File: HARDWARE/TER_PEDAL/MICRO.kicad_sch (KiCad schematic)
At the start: 23 parts, among them J7 DEBUG, SW1 RST, U1 STM32F103C8Tx, Y1 8mHz

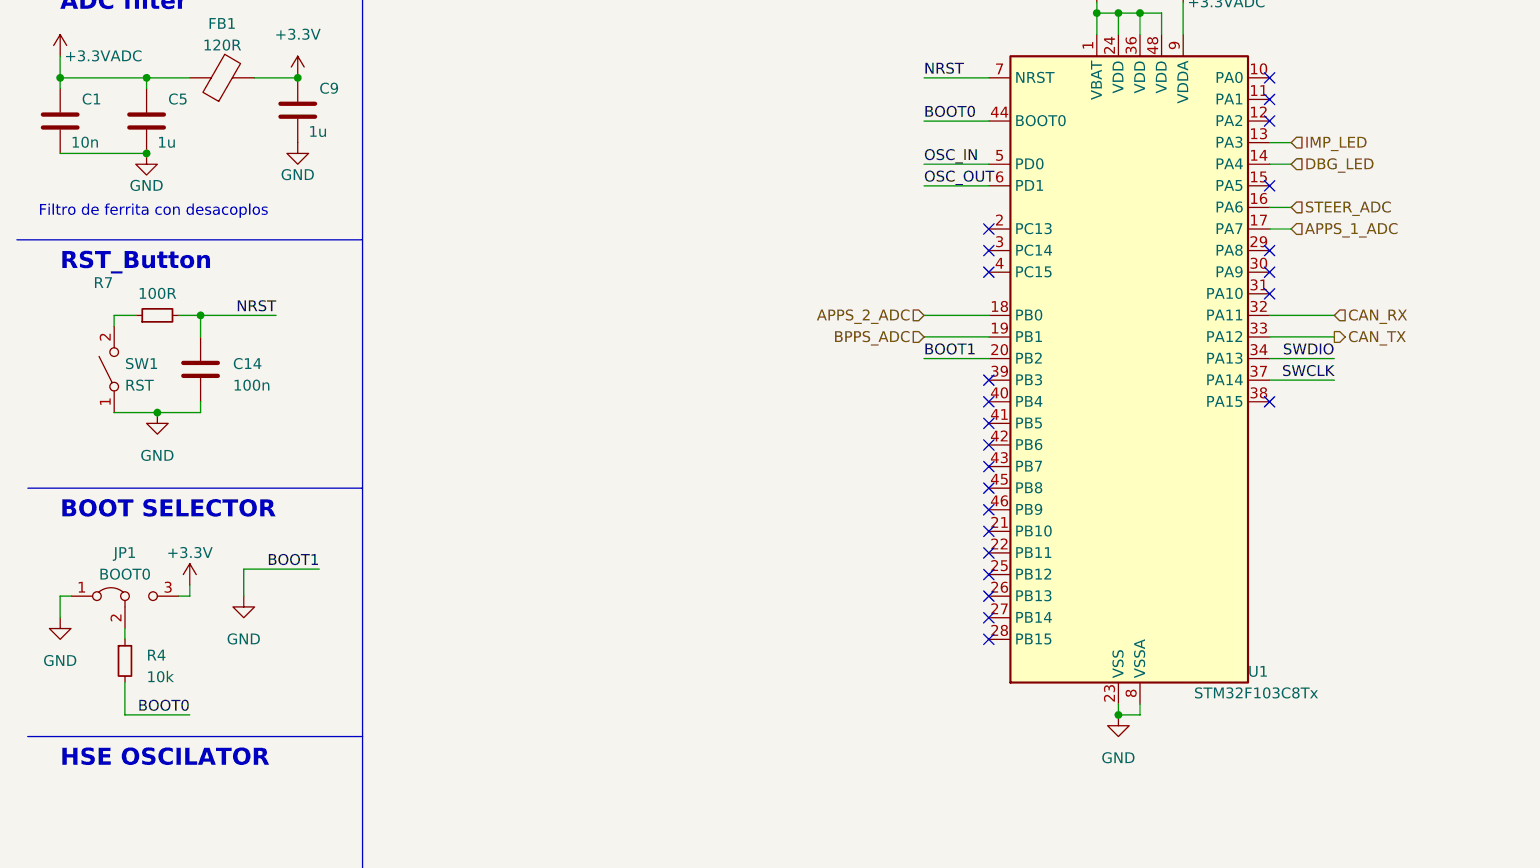
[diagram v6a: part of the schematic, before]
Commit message: Added voltage followers to sensing, improved can circuitri, improved layout, waiting for routing
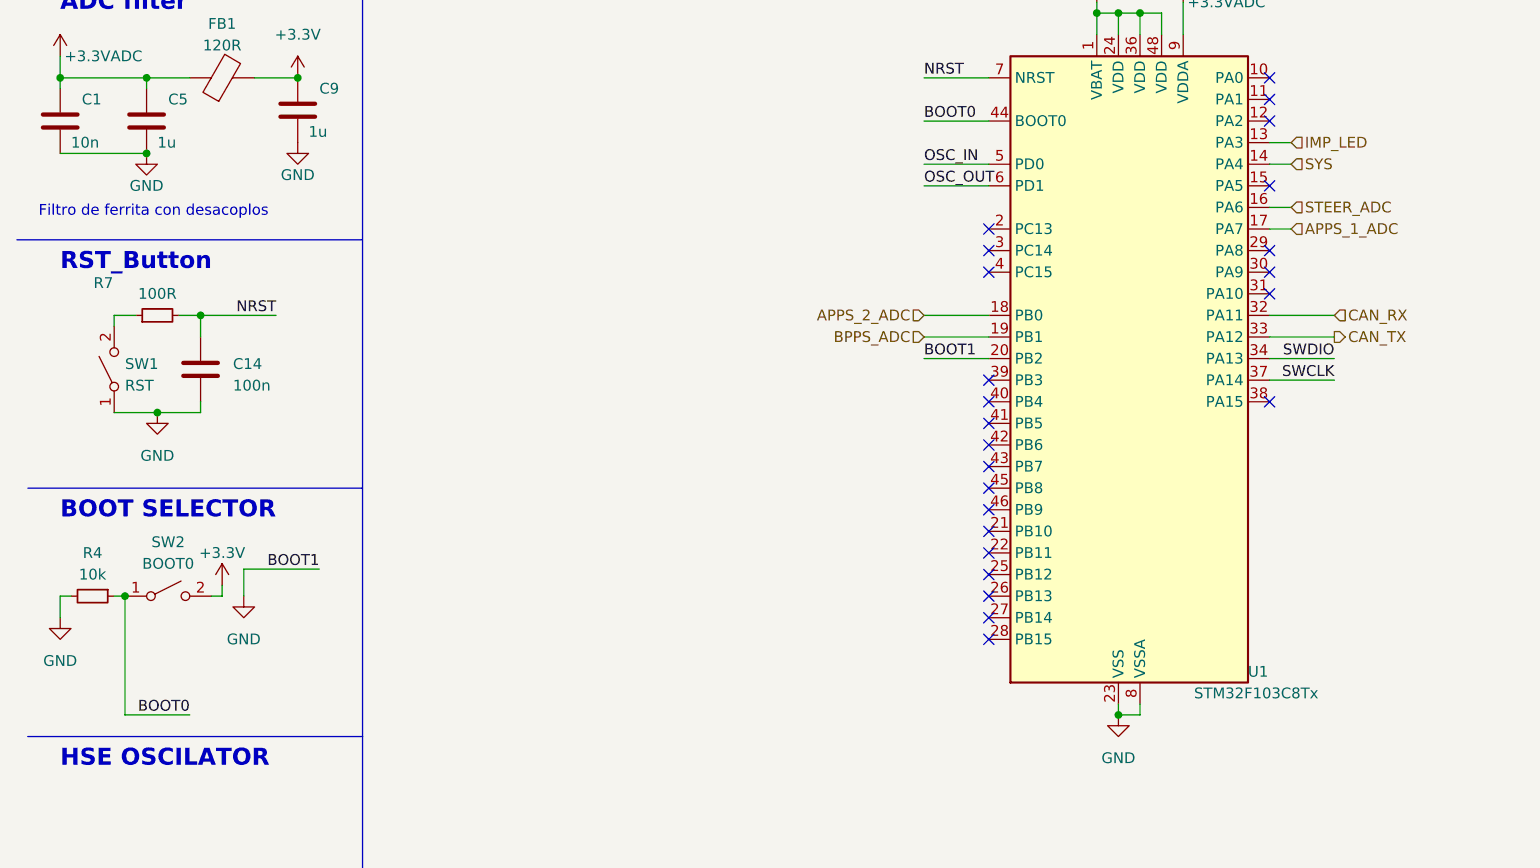
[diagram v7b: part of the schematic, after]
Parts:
- removed JP1: BOOT0, Connector_PinHeader_2.00mm:PinHeader_1x03_P2.00mm_Vertical, symbol Jumper:Jumper_3_Bridged12
- added SW2: BOOT0, Button_Switch_SMD:SW_SPST_PTS810, symbol Switch:SW_SPST
- SW1: footprint Button_Switch_SMD:SW_Tactile_SPST_NO_Straight_CK_PTS636Sx25SMTRLFS -> Button_Switch_SMD:SW_SPST_PTS810
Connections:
- net +3.3V: now also SW2.2 (B)
- net BOOT0: now also R4.1, SW2.1 (A); no longer R4.2
- net GND: now also R4.2
- net DBG_LED renamed SYS
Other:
- company: (none) -> Tecnun-eRacing
- title: (none) -> TeR_PEDAL
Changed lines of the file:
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@@
 	(generator_version "8.0")
 	(paper "A4")
+	(title_block
+		(title "TeR_PEDAL")
+		(date "2023-11-24")
+		(rev "V1.1.0")
+		(company "Tecnun-eRacing")
+		(comment 1 "Ozuba")
+	)
 	(junction
 		(at 15.24 25.4)
@@
 	)
 	(junction
+		(at 24.13 111.76)
+		(diameter 0)
+		(color 0 0 0 0)
+	)
+	(junction
 		(at 38.1 25.4)
 		(diameter 0)
@@
 	(wire
 		(pts
+			(xy 35.56 111.76) (xy 34.29 111.76)
+		)
+		(stroke
+			(width 0)
+			(type default)
+		)
+	)
+	(wire
+		(pts
 			(xy 46.99 165.1) (xy 46.99 157.48)
 		)
@@
 	(wire
 		(pts
-			(xy 31.75 110.49) (xy 31.75 111.76)
+			(xy 35.56 110.49) (xy 35.56 111.76)
 		)
 		(stroke
@@
 	(wire
 		(pts
+			(xy 24.13 111.76) (xy 24.13 125.73)
+		)
+		(stroke
+			(width 0)
+			(type default)
+		)
+	)
+	(wire
+		(pts
 			(xy 256.54 31.75) (xy 256.54 33.02)
 		)
@@
 	(wire
 		(pts
-			(xy 31.75 111.76) (xy 30.48 111.76)
+			(xy 24.13 111.76) (xy 22.86 111.76)
 		)
 		(stroke
@@
 	(wire
 		(pts
-			(xy 24.13 115.57) (xy 24.13 116.84)
-		)
-		(stroke
-			(width 0)
-			(type default)
-		)
-	)
-	(wire
-		(pts
 			(xy 140.97 124.46) (xy 140.97 125.73)
 		)
@@
 	(wire
 		(pts
-			(xy 24.13 121.92) (xy 24.13 125.73)
-		)
-		(stroke
-			(width 0)
-			(type default)
-		)
-	)
-	(wire
-		(pts
 			(xy 33.02 90.17) (xy 27.94 90.17)
 		)
@@
 		)
 	)
-	(hierarchical_label "DBG_LED"
+	(hierarchical_label "SYS"
 		(shape input)
 		(at 161.29 60.96 0)
@@
 	)
 	(symbol
-		(lib_id "Jumper:Jumper_3_Bridged12")
-		(at 24.13 111.76 0)
-		(unit 1)
-		(exclude_from_sim no)
-		(in_bom yes)
-		(on_board yes)
-		(dnp no)
-		(fields_autoplaced yes)
-		(property "Reference" "JP1"
-			(at 24.13 106.68 0)
-			(effects
-				(font
-					(size 1.27 1.27)
-				)
-			)
-		)
-		(property "Value" "BOOT0"
-			(at 24.13 109.22 0)
-			(effects
-				(font
-					(size 1.27 1.27)
-				)
-			)
-		)
-		(property "Footprint" "Connector_PinHeader_2.00mm:PinHeader_1x03_P2.00mm_Vertical"
-			(at 24.13 111.76 0)
-			(effects
-				(font
-					(size 1.27 1.27)
-				)
-				(hide yes)
-			)
-		)
-		(property "Datasheet" "~"
-			(at 24.13 111.76 0)
-			(effects
-				(font
-					(size 1.27 1.27)
-				)
-				(hide yes)
-			)
-		)
-		(property "Description" ""
-			(at 24.13 111.76 0)
-			(effects
-				(font
-					(size 1.27 1.27)
-				)
-				(hide yes)
-			)
-		)
-		(pin "1"
-		)
-		(pin "2"
-		)
-		(pin "3"
-		)
-		(instances
-			(project "TER_PEDAL"
-				(path "/73ede3a3-6344-40fe-9207-10ff50d388ba/7632a94a-0691-4527-83e2-6d814eae7e64"
-					(reference "JP1")
-					(unit 1)
-				)
-			)
-		)
-	)
-	(symbol
 		(lib_id "MCU_ST_STM32F1:STM32F103C8Tx")
 		(at 140.97 86.36 0)
@@
 	(symbol
 		(lib_id "power:+3.3V")
-		(at 31.75 110.49 0)
+		(at 35.56 110.49 0)
 		(unit 1)
 		(exclude_from_sim no)
@@
 		(fields_autoplaced yes)
 		(property "Reference" "#PWR024"
-			(at 31.75 114.3 0)
+			(at 35.56 114.3 0)
 			(effects
 				(font
@@
 		)
 		(property "Value" "+3.3V"
-			(at 31.75 106.68 0)
+			(at 35.56 106.68 0)
 			(effects
 				(font
@@
 		)
 		(property "Footprint" ""
-			(at 31.75 110.49 0)
+			(at 35.56 110.49 0)
 			(effects
 				(font
@@
 		)
 		(property "Datasheet" ""
-			(at 31.75 110.49 0)
+			(at 35.56 110.49 0)
 			(effects
 				(font
@@
 		)
 		(property "Description" ""
-			(at 31.75 110.49 0)
+			(at 35.56 110.49 0)
 			(effects
 				(font
@@
 	)
 	(symbol
+		(lib_id "Device:R_Small")
+		(at 20.32 111.76 270)
+		(unit 1)
+		(exclude_from_sim no)
+		(in_bom yes)
+		(on_board yes)
+		(dnp no)
+		(fields_autoplaced yes)
+		(property "Reference" "R4"
+			(at 20.32 106.68 90)
+			(effects
+				(font
+					(size 1.27 1.27)
+				)
+			)
+		)
+		(property "Value" "10k"
+			(at 20.32 109.22 90)
+			(effects
+				(font
+					(size 1.27 1.27)
+				)
+			)
+		)
+		(property "Footprint" "Resistor_SMD:R_0603_1608Metric"
+			(at 20.32 111.76 0)
+			(effects
+				(font
+					(size 1.27 1.27)
+				)
+				(hide yes)
+			)
+		)
+		(property "Datasheet" "~"
+			(at 20.32 111.76 0)
+			(effects
+				(font
+					(size 1.27 1.27)
+				)
+				(hide yes)
+			)
+		)
+		(property "Description" ""
+			(at 20.32 111.76 0)
+			(effects
+				(font
+					(size 1.27 1.27)
+				)
+				(hide yes)
+			)
+		)
+		(pin "1"
+		)
+		(pin "2"
+		)
+		(instances
+			(project "TER_PEDAL"
+				(path "/73ede3a3-6344-40fe-9207-10ff50d388ba/7632a94a-0691-4527-83e2-6d814eae7e64"
+					(reference "R4")
+					(unit 1)
+				)
+			)
+		)
+	)
+	(symbol
 		(lib_id "power:GND")
 		(at 46.99 165.1 0)
@@
 			)
 		)
-		(property "Footprint" "Button_Switch_SMD:SW_Tactile_SPST_NO_Straight_CK_PTS636Sx25SMTRLFS"
+		(property "Footprint" "Button_Switch_SMD:SW_SPST_PTS810"
 			(at 22.86 85.09 0)
 			(effects
@@
 	)
 	(symbol
-		(lib_id "Device:R_Small")
-		(at 24.13 119.38 0)
-		(unit 1)
-		(exclude_from_sim no)
-		(in_bom yes)
-		(on_board yes)
-		(dnp no)
-		(fields_autoplaced yes)
-		(property "Reference" "R4"
-			(at 26.67 118.745 0)
-			(effects
-				(font
-					(size 1.27 1.27)
-				)
-				(justify left)
-			)
-		)
-		(property "Value" "10k"
-			(at 26.67 121.285 0)
-			(effects
-				(font
-					(size 1.27 1.27)
-				)
-				(justify left)
-			)
-		)
-		(property "Footprint" "Resistor_SMD:R_0603_1608Metric"
-			(at 24.13 119.38 0)
-			(effects
-				(font
-					(size 1.27 1.27)
-				)
-				(hide yes)
-			)
-		)
-		(property "Datasheet" "~"
-			(at 24.13 119.38 0)
-			(effects
-				(font
-					(size 1.27 1.27)
-				)
-				(hide yes)
-			)
-		)
-		(property "Description" ""
-			(at 24.13 119.38 0)
-			(effects
-				(font
-					(size 1.27 1.27)
-				)
-				(hide yes)
-			)
-		)
-		(pin "1"
-		)
-		(pin "2"
-		)
-		(instances
-			(project "TER_PEDAL"
-				(path "/73ede3a3-6344-40fe-9207-10ff50d388ba/7632a94a-0691-4527-83e2-6d814eae7e64"
-					(reference "R4")
-					(unit 1)
-				)
-			)
-		)
-	)
-	(symbol
 		(lib_id "power:+3.3V")
 		(at 275.59 40.64 270)
@@
 					(unit 1)
 				)
+			)
+		)
+	)
+	(symbol
+		(lib_id "Switch:SW_SPST")
+		(at 29.21 111.76 0)
+		(unit 1)
+		(exclude_from_sim no)
+		(in_bom yes)
+		(on_board yes)
+		(dnp no)
+		(fields_autoplaced yes)
+		(property "Reference" "SW2"
+			(at 29.21 105.41 0)
+			(effects
+				(font
+					(size 1.27 1.27)
+				)
+			)
+		)
+		(property "Value" "BOOT0"
+			(at 29.21 107.95 0)
+			(effects
+				(font
+					(size 1.27 1.27)
+				)
+			)
+		)
+		(property "Footprint" "Button_Switch_SMD:SW_SPST_PTS810"
+			(at 29.21 111.76 0)
+			(effects
+				(font
+					(size 1.27 1.27)
+				)
+				(hide yes)
+			)
+		)
+		(property "Datasheet" "~"
+			(at 29.21 111.76 0)
+			(effects
+				(font
+					(size 1.27 1.27)
+				)
+				(hide yes)
+			)
+		)
+		(property "Description" ""
+			(at 29.21 111.76 0)
+			(effects
+				(font
+					(size 1.27 1.27)
+				)
+				(hide yes)
+			)
+		)
+		(pin "1"
+		)
+		(pin "2"
+		)
+		(instances
+			(project "TER_PEDAL"
+				(path "/73ede3a3-6344-40fe-9207-10ff50d388ba/7632a94a-0691-4527-83e2-6d814eae7e64"
+					(reference "SW2")
+					(unit 1)
+				)

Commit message: Añadiendo eeprom (no terminado)
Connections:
- net SCL: now reaches U1.42 (PB6)
- net SDA: now reaches U1.43 (PB7)
- no-connect marks 25 -> 23
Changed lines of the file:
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@@
-	)
-	(no_connect
-		(at 125.73 96.52)
 	)
 	(no_connect
@@
 	)
 	(no_connect
-		(at 125.73 93.98)
-	)
-	(no_connect
 		(at 125.73 114.3)
 	)
@@
 	)
 	(no_connect
+		(at 125.73 104.14)
+	)
+	(no_connect
 		(at 125.73 91.44)
 	)
@@
 	)
 	(no_connect
+		(at 125.73 106.68)
+	)
+	(no_connect
 		(at 158.75 88.9)
 	)
@@
 	)
 	(no_connect
-		(at 125.73 106.68)
-	)
-	(no_connect
 		(at 125.73 109.22)
 	)
 	(no_connect
-		(at 125.73 104.14)
-	)
-	(no_connect
 		(at 256.54 45.72)
 	)
@@
 	(wire
 		(pts
+			(xy 121.92 96.52) (xy 125.73 96.52)
+		)
+		(stroke
+			(width 0)
+			(type default)
+		)
+	)
+	(wire
+		(pts
 			(xy 16.51 48.26) (xy 16.51 50.8)
 		)
@@
 		(pts
 			(xy 143.51 124.46) (xy 143.51 125.73)
+		)
+		(stroke
+			(width 0)
+			(type default)
+		)
+	)
+	(wire
+		(pts
+			(xy 121.92 93.98) (xy 125.73 93.98)
 		)
 		(stroke
@@
 		)
 	)
+	(hierarchical_label "SCL"
+		(shape input)
+		(at 121.92 93.98 180)
+		(fields_autoplaced yes)
+		(effects
+			(font
+				(size 1.27 1.27)
+			)
+			(justify right)
+		)
+	)
+	(hierarchical_label "SDA"
+		(shape input)
+		(at 121.92 96.52 180)
+		(fields_autoplaced yes)
+		(effects
+			(font
+				(size 1.27 1.27)
+			)
+			(justify right)
+		)
+	)
